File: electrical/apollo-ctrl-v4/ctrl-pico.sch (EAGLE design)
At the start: 47 parts, among them J1 ESP32-PICO-KIT, J2 DNP, J3 DNP, J4 DNP, J6 DISPLAY_RIGHT, J7 DISPLAY_LEFT, Q1 SOT23-3, U1 DNP (24LC01)

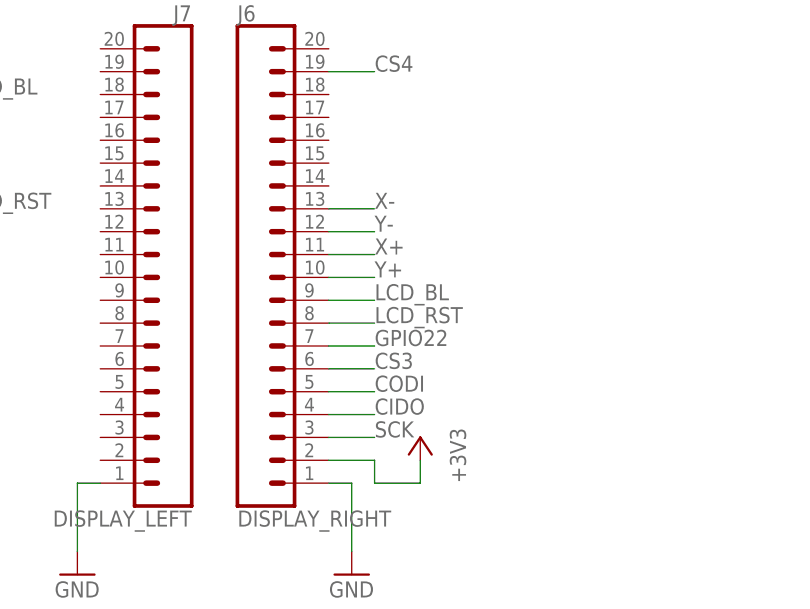
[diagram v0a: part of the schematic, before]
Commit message: Update TFT LCD pinout for version 2 of the Adafruit breakout board
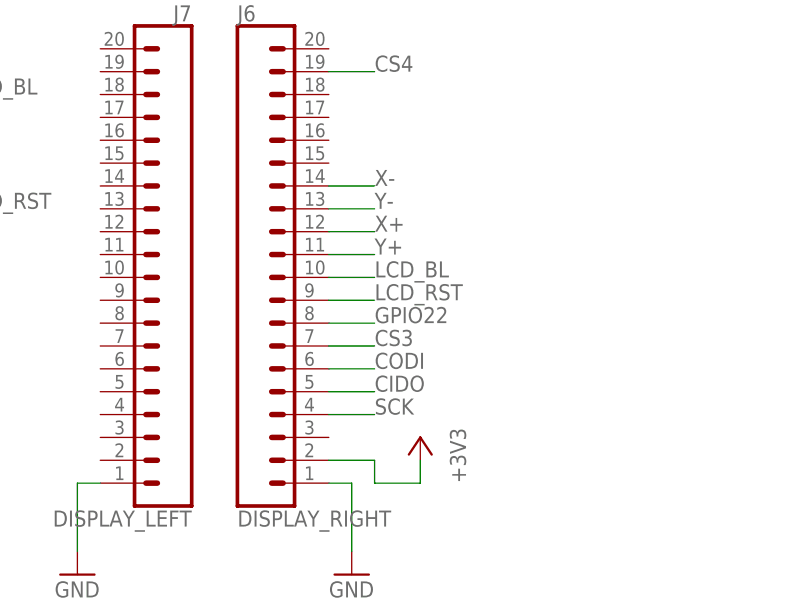
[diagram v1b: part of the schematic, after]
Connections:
- net CIDO: now also J6.5; no longer J6.4
- net CODI: now also J6.6; no longer J6.5
- net CS3: now also J6.7; no longer J6.6
- net GPIO22: now also J6.8; no longer J6.7
- net LCD_BL: now also J6.10; no longer J6.9
- net LCD_RST: now also J6.9; no longer J6.8
- net SCK: now also J6.4; no longer J6.3
- net X+: now also J6.12; no longer J6.11
- net X-: now also J6.14; no longer J6.13
- net Y+: now also J6.11; no longer J6.10
- net Y-: now also J6.13; no longer J6.12
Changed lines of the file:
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@@
 <drawing>
 <settings>
-<setting alwaysvectorfont="no"/>
+<setting alwaysvectorfont="yes"/>
 <setting keepoldvectorfont="yes"/>
 <setting verticaltext="up"/>
@@
 </segment>
 <segment>
-<pinref part="J6" gate="G$1" pin="3"/>
-<wire x1="314.96" y1="134.62" x2="320.04" y2="134.62" width="0.1524" layer="91"/>
-<label x="320.04" y="134.62" size="1.778" layer="95"/>
+<wire x1="314.96" y1="137.16" x2="320.04" y2="137.16" width="0.1524" layer="91"/>
+<label x="320.04" y="137.16" size="1.778" layer="95"/>
+<pinref part="J6" gate="G$1" pin="4"/>
 </segment>
 </net>
@@
 </segment>
 <segment>
-<pinref part="J6" gate="G$1" pin="5"/>
-<wire x1="320.04" y1="139.7" x2="314.96" y2="139.7" width="0.1524" layer="91"/>
-<label x="320.04" y="139.7" size="1.778" layer="95"/>
+<wire x1="320.04" y1="142.24" x2="314.96" y2="142.24" width="0.1524" layer="91"/>
+<label x="320.04" y="142.24" size="1.778" layer="95"/>
+<pinref part="J6" gate="G$1" pin="6"/>
 </segment>
 </net>
@@
 </segment>
 <segment>
-<pinref part="J6" gate="G$1" pin="4"/>
-<wire x1="314.96" y1="137.16" x2="320.04" y2="137.16" width="0.1524" layer="91"/>
-<label x="320.04" y="137.16" size="1.778" layer="95"/>
+<wire x1="314.96" y1="139.7" x2="320.04" y2="139.7" width="0.1524" layer="91"/>
+<label x="320.04" y="139.7" size="1.778" layer="95"/>
+<pinref part="J6" gate="G$1" pin="5"/>
 </segment>
 </net>
@@
 </segment>
 <segment>
-<pinref part="J6" gate="G$1" pin="6"/>
-<wire x1="320.04" y1="142.24" x2="314.96" y2="142.24" width="0.1524" layer="91"/>
-<label x="320.04" y="142.24" size="1.778" layer="95"/>
+<wire x1="320.04" y1="144.78" x2="314.96" y2="144.78" width="0.1524" layer="91"/>
+<label x="320.04" y="144.78" size="1.778" layer="95"/>
+<pinref part="J6" gate="G$1" pin="7"/>
 </segment>
 </net>
@@
 </segment>
 <segment>
-<pinref part="J6" gate="G$1" pin="7"/>
-<wire x1="320.04" y1="144.78" x2="314.96" y2="144.78" width="0.1524" layer="91"/>
-<label x="320.04" y="144.78" size="1.778" layer="95"/>
+<wire x1="320.04" y1="147.32" x2="314.96" y2="147.32" width="0.1524" layer="91"/>
+<label x="320.04" y="147.32" size="1.778" layer="95"/>
+<pinref part="J6" gate="G$1" pin="8"/>
 </segment>
 </net>
@@
 </segment>
 <segment>
-<pinref part="J6" gate="G$1" pin="9"/>
-<wire x1="320.04" y1="149.86" x2="314.96" y2="149.86" width="0.1524" layer="91"/>
-<label x="320.04" y="149.86" size="1.778" layer="95"/>
+<wire x1="320.04" y1="152.4" x2="314.96" y2="152.4" width="0.1524" layer="91"/>
+<label x="320.04" y="152.4" size="1.778" layer="95"/>
+<pinref part="J6" gate="G$1" pin="10"/>
 </segment>
 </net>
@@
 </segment>
 <segment>
-<pinref part="J6" gate="G$1" pin="8"/>
-<wire x1="320.04" y1="147.32" x2="314.96" y2="147.32" width="0.1524" layer="91"/>
-<label x="320.04" y="147.32" size="1.778" layer="95"/>
+<wire x1="320.04" y1="149.86" x2="314.96" y2="149.86" width="0.1524" layer="91"/>
+<label x="320.04" y="149.86" size="1.778" layer="95"/>
+<pinref part="J6" gate="G$1" pin="9"/>
 </segment>
 </net>
 <net name="Y+" class="0">
 <segment>
-<pinref part="J6" gate="G$1" pin="10"/>
-<wire x1="320.04" y1="152.4" x2="314.96" y2="152.4" width="0.1524" layer="91"/>
-<label x="320.04" y="152.4" size="1.778" layer="95"/>
-</segment>
-</net>
-<net name="X+" class="0">
-<segment>
-<pinref part="J6" gate="G$1" pin="11"/>
 <wire x1="320.04" y1="154.94" x2="314.96" y2="154.94" width="0.1524" layer="91"/>
 <label x="320.04" y="154.94" size="1.778" layer="95"/>
-</segment>
-</net>
-<net name="Y-" class="0">
-<segment>
-<pinref part="J6" gate="G$1" pin="12"/>
+<pinref part="J6" gate="G$1" pin="11"/>
+</segment>
+</net>
+<net name="X+" class="0">
+<segment>
 <wire x1="320.04" y1="157.48" x2="314.96" y2="157.48" width="0.1524" layer="91"/>
 <label x="320.04" y="157.48" size="1.778" layer="95"/>
-</segment>
-</net>
-<net name="X-" class="0">
-<segment>
-<pinref part="J6" gate="G$1" pin="13"/>
+<pinref part="J6" gate="G$1" pin="12"/>
+</segment>
+</net>
+<net name="Y-" class="0">
+<segment>
 <wire x1="320.04" y1="160.02" x2="314.96" y2="160.02" width="0.1524" layer="91"/>
 <label x="320.04" y="160.02" size="1.778" layer="95"/>
-</segment>
-</net>
+<pinref part="J6" gate="G$1" pin="13"/>
+</segment>
+</net>
+<net name="X-" class="0">
+<segment>
+<wire x1="320.04" y1="162.56" x2="314.96" y2="162.56" width="0.1524" layer="91"/>
+<label x="320.04" y="162.56" size="1.778" layer="95"/>
+<pinref part="J6" gate="G$1" pin="14"/>
+</segment>
+</net>

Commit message: Add touch screen connectors on control PCB, and roll up fab to B
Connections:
- removed net CS5: J1.IO26, JP1.1, R10.1, U$1.PIN7
- removed net SCL2: J1.IO19
- removed net SDA2: J1.IO18
- removed net X+: J6.12
- removed net X-: J6.14
- removed net Y+: J6.11
- removed net Y-: J6.13
- new net ADC5: J1.IO34, J6.11
- new net BUZ: J1.IO19, Q1.G, R24.2
- new net LCD_CD: J1.IO18, J6.8, R10.1
- net ADC2: now also J1.IO26, J6.12; no longer J1.IO35, Q1.G, R24.2
- net ADC3: now also J6.14; no longer U$1.PIN34
- net ADC4: now also J6.13; no longer U$1.PIN35
- net GPIO22: now also JP1.1; no longer J6.8
- net VMON: now also J1.IO35; no longer J1.IO34
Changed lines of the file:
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@@
+</segment>
+<segment>
+<wire x1="320.04" y1="144.78" x2="314.96" y2="144.78" width="0.1524" layer="91"/>
+<label x="320.04" y="144.78" size="1.778" layer="95"/>
+<pinref part="J6" gate="G$1" pin="7"/>
 </segment>
 <segment>
@@
 <label x="20.32" y="45.72" size="1.778" layer="95"/>
 </segment>
-<segment>
-<wire x1="320.04" y1="144.78" x2="314.96" y2="144.78" width="0.1524" layer="91"/>
-<label x="320.04" y="144.78" size="1.778" layer="95"/>
-<pinref part="J6" gate="G$1" pin="7"/>
-</segment>
-</net>
-<net name="CS5" class="0">
-<segment>
-<pinref part="U$1" gate="G$1" pin="PIN7"/>
-<wire x1="93.98" y1="162.56" x2="106.68" y2="162.56" width="0.1524" layer="91"/>
-<label x="93.98" y="162.56" size="1.778" layer="95"/>
-</segment>
-<segment>
-<pinref part="R10" gate="G$1" pin="1"/>
-<wire x1="12.7" y1="162.56" x2="7.62" y2="162.56" width="0.1524" layer="91"/>
-<wire x1="7.62" y1="162.56" x2="7.62" y2="165.1" width="0.1524" layer="91"/>
-<label x="10.16" y="162.56" size="1.778" layer="95"/>
-</segment>
-<segment>
-<pinref part="J1" gate="G$1" pin="IO26"/>
-<wire x1="20.32" y1="50.8" x2="33.02" y2="50.8" width="0.1524" layer="91"/>
-<label x="20.32" y="50.8" size="1.778" layer="95"/>
-</segment>
-<segment>
-<pinref part="JP1" gate="G$1" pin="1"/>
-<wire x1="254" y1="172.72" x2="261.62" y2="172.72" width="0.1524" layer="91"/>
-<label x="254" y="172.72" size="1.778" layer="95"/>
+</net>
+<net name="ADC5" class="0">
+<segment>
+<label x="320.04" y="154.94" size="1.778" layer="95"/>
+<pinref part="J6" gate="G$1" pin="11"/>
+<wire x1="314.96" y1="154.94" x2="320.04" y2="154.94" width="0.1524" layer="91"/>
+</segment>
+<segment>
+<pinref part="J1" gate="G$1" pin="IO34"/>
+<wire x1="20.32" y1="40.64" x2="33.02" y2="40.64" width="0.1524" layer="91"/>
+<label x="20.32" y="40.64" size="1.778" layer="95"/>
 </segment>
 </net>
@@
 <wire x1="17.78" y1="78.74" x2="17.78" y2="76.2" width="0.1524" layer="91"/>
 <pinref part="R6" gate="G$1" pin="2"/>
+<label x="20.32" y="78.74" size="1.778" layer="95"/>
 </segment>
 </net>
@@
 <wire x1="17.78" y1="81.28" x2="17.78" y2="83.82" width="0.1524" layer="91"/>
 <pinref part="R5" gate="G$1" pin="2"/>
+<label x="20.32" y="81.28" size="1.778" layer="95"/>
 </segment>
 </net>
@@
 </net>
 <net name="VMON" class="0">
-<segment>
-<pinref part="J1" gate="G$1" pin="IO34"/>
-<wire x1="20.32" y1="40.64" x2="33.02" y2="40.64" width="0.1524" layer="91"/>
-<label x="20.32" y="40.64" size="1.778" layer="95"/>
-</segment>
 <segment>
 <pinref part="R19" gate="G$1" pin="2"/>
@@
 <label x="124.46" y="91.44" size="1.778" layer="95"/>
 </segment>
-</net>
-<net name="ADC2" class="0">
 <segment>
 <pinref part="J1" gate="G$1" pin="IO35"/>
@@
 <label x="20.32" y="38.1" size="1.778" layer="95"/>
 </segment>
-<segment>
-<pinref part="Q1" gate="NMOS" pin="G"/>
-<wire x1="40.64" y1="116.84" x2="27.94" y2="116.84" width="0.1524" layer="91"/>
-<label x="30.48" y="116.84" size="1.778" layer="95"/>
-<pinref part="R24" gate="G$1" pin="2"/>
+</net>
+<net name="ADC2" class="0">
+<segment>
+<pinref part="J1" gate="G$1" pin="IO26"/>
+<wire x1="20.32" y1="50.8" x2="33.02" y2="50.8" width="0.1524" layer="91"/>
+<label x="20.32" y="50.8" size="1.778" layer="95"/>
+</segment>
+<segment>
+<label x="320.04" y="157.48" size="1.778" layer="95"/>
+<pinref part="J6" gate="G$1" pin="12"/>
+<wire x1="314.96" y1="157.48" x2="320.04" y2="157.48" width="0.1524" layer="91"/>
 </segment>
 </net>
@@
 </segment>
 <segment>
-<pinref part="U$1" gate="G$1" pin="PIN34"/>
-<wire x1="167.64" y1="160.02" x2="160.02" y2="160.02" width="0.1524" layer="91"/>
-<label x="165.1" y="160.02" size="1.778" layer="95"/>
+<label x="320.04" y="162.56" size="1.778" layer="95"/>
+<wire x1="314.96" y1="162.56" x2="320.04" y2="162.56" width="0.1524" layer="91"/>
+<pinref part="J6" gate="G$1" pin="14"/>
 </segment>
 </net>
@@
 </segment>
 <segment>
-<pinref part="U$1" gate="G$1" pin="PIN35"/>
-<wire x1="167.64" y1="157.48" x2="160.02" y2="157.48" width="0.1524" layer="91"/>
-<label x="165.1" y="157.48" size="1.778" layer="95"/>
+<label x="320.04" y="160.02" size="1.778" layer="95"/>
+<pinref part="J6" gate="G$1" pin="13"/>
+<wire x1="314.96" y1="160.02" x2="320.04" y2="160.02" width="0.1524" layer="91"/>
 </segment>
 </net>
@@
 </segment>
 <segment>
-<wire x1="320.04" y1="147.32" x2="314.96" y2="147.32" width="0.1524" layer="91"/>
-<label x="320.04" y="147.32" size="1.778" layer="95"/>
-<pinref part="J6" gate="G$1" pin="8"/>
+<pinref part="JP1" gate="G$1" pin="1"/>
+<wire x1="254" y1="172.72" x2="261.62" y2="172.72" width="0.1524" layer="91"/>
+<label x="254" y="172.72" size="1.778" layer="95"/>
 </segment>
 </net>
@@
 </segment>
 </net>
-<net name="SDA2" class="0">
+<net name="LCD_CD" class="0">
+<segment>
+<wire x1="320.04" y1="147.32" x2="314.96" y2="147.32" width="0.1524" layer="91"/>
+<label x="320.04" y="147.32" size="1.778" layer="95"/>
+<pinref part="J6" gate="G$1" pin="8"/>
+</segment>
+<segment>
+<pinref part="R10" gate="G$1" pin="1"/>
+<wire x1="12.7" y1="160.02" x2="7.62" y2="160.02" width="0.1524" layer="91"/>
+<wire x1="7.62" y1="160.02" x2="7.62" y2="165.1" width="0.1524" layer="91"/>
+<label x="10.16" y="160.02" size="1.778" layer="95"/>
+</segment>
 <segment>
 <pinref part="J1" gate="G$1" pin="IO18"/>
 <wire x1="20.32" y1="66.04" x2="33.02" y2="66.04" width="0.1524" layer="91"/>
 <label x="20.32" y="66.04" size="1.778" layer="95"/>
-</segment>
-</net>
-<net name="SCL2" class="0">
-<segment>
-<pinref part="J1" gate="G$1" pin="IO19"/>
-<wire x1="20.32" y1="63.5" x2="33.02" y2="63.5" width="0.1524" layer="91"/>
-<label x="20.32" y="63.5" size="1.778" layer="95"/>
 </segment>
 </net>
@@
 <label x="320.04" y="149.86" size="1.778" layer="95"/>
 <pinref part="J6" gate="G$1" pin="9"/>
-</segment>
-</net>
-<net name="Y+" class="0">
-<segment>
-<wire x1="320.04" y1="154.94" x2="314.96" y2="154.94" width="0.1524" layer="91"/>
-<label x="320.04" y="154.94" size="1.778" layer="95"/>
-<pinref part="J6" gate="G$1" pin="11"/>
-</segment>
-</net>
-<net name="X+" class="0">
-<segment>
-<wire x1="320.04" y1="157.48" x2="314.96" y2="157.48" width="0.1524" layer="91"/>
-<label x="320.04" y="157.48" size="1.778" layer="95"/>
-<pinref part="J6" gate="G$1" pin="12"/>
-</segment>
-</net>
-<net name="Y-" class="0">
-<segment>
-<wire x1="320.04" y1="160.02" x2="314.96" y2="160.02" width="0.1524" layer="91"/>
-<label x="320.04" y="160.02" size="1.778" layer="95"/>
-<pinref part="J6" gate="G$1" pin="13"/>
-</segment>
-</net>
-<net name="X-" class="0">
-<segment>
-<wire x1="320.04" y1="162.56" x2="314.96" y2="162.56" width="0.1524" layer="91"/>
-<label x="320.04" y="162.56" size="1.778" layer="95"/>
-<pinref part="J6" gate="G$1" pin="14"/>
 </segment>
 </net>
@@
 </segment>
 </net>
+<net name="BUZ" class="0">
+<segment>
+<pinref part="Q1" gate="NMOS" pin="G"/>
+<wire x1="40.64" y1="116.84" x2="27.94" y2="116.84" width="0.1524" layer="91"/>
+<label x="30.48" y="116.84" size="1.778" layer="95"/>
+<pinref part="R24" gate="G$1" pin="2"/>
+</segment>
+<segment>
+<pinref part="J1" gate="G$1" pin="IO19"/>
+<wire x1="20.32" y1="63.5" x2="33.02" y2="63.5" width="0.1524" layer="91"/>
+<label x="20.32" y="63.5" size="1.778" layer="95"/>
+</segment>
+</net>
